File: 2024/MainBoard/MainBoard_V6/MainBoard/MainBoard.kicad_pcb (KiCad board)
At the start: 2 copper layers, 130.5 x 65 mm, 90 parts, among them J1 Raspberry_Pi_2_3, J14 UART, J15 TFT3, J16 CAN_CON, J2 fan, J3 USB_C_Receptacle_USB2.0_16P, J4 metor, J6 Debug, J8 MOLEX MINISPOX, Q1 Q_NMOS_GSD, Q2 Q_NMOS_GSD, SW1 SW_MEC_5E, SW2 Ras_1, SW3 Ras_2, SW4 SW_Wuerth_450301014042, SW5 SW_MEC_5E, SW6 SW_MEC_5E, U1 STM32F446RETx, U10 MPU9250, U11 LM1084-5.0, U2 CH340E, U3 MOUDLE-SEEEDUINO-XIAO, U6 BNO055, U7 AZ1117-3.3, U8 MAX3051, Y1 CSTNE16M0V530000R0

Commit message: 完成
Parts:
- J14: moved to B.Cu
- moved J14 6.00 mm to (43.5, 25.8), turned to 180 degrees
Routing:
- net GND: track 804.0 -> 796.6 mm, vias 69 -> 97
- net +3.3V: track 284.9 -> 290.9 mm
- net UART2_RX: track 38.8 -> 43.8 mm
- net T_CS: track 25.7 -> 26.7 mm
- net UART2_TX: track 39.0 -> 38.3 mm
- added copper zone on B.Cu, net +5V
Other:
- board text added: "16V GND"
- board text added: "5.1k"
- board text added: "D"
- board text added: "Discharge"
- board text added: "MainBoard v6"
- board text added: "← → USB SWD"
- board text removed: "MainBoard v5"
- board text removed: "USB← →SWD"

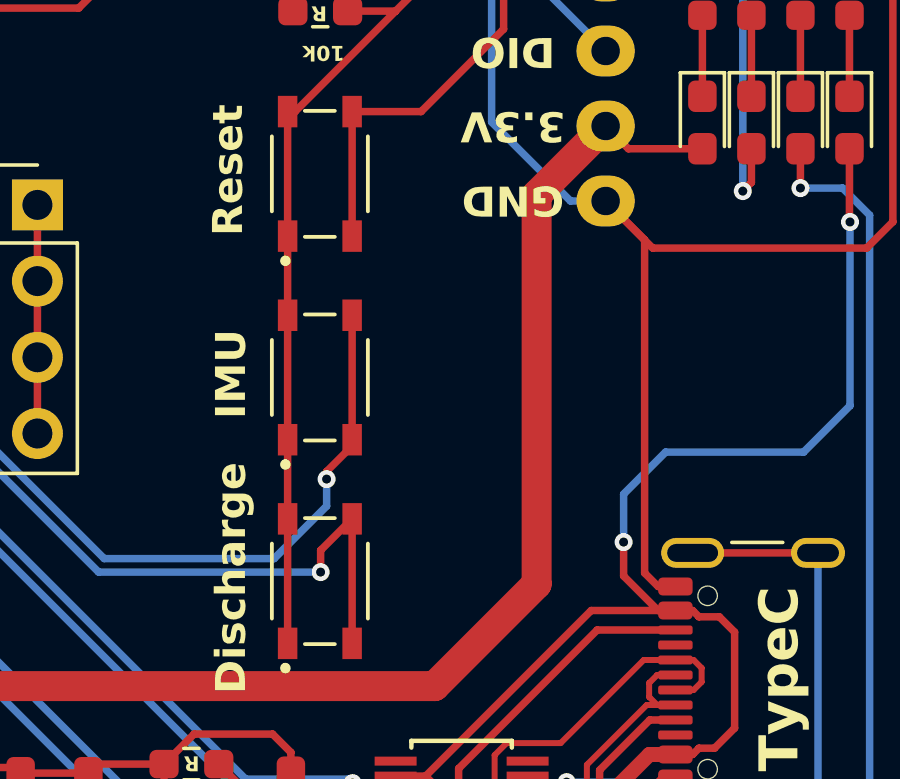
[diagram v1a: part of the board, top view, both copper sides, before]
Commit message: 差し替えver
リセットにプルアップ抵抗いれた
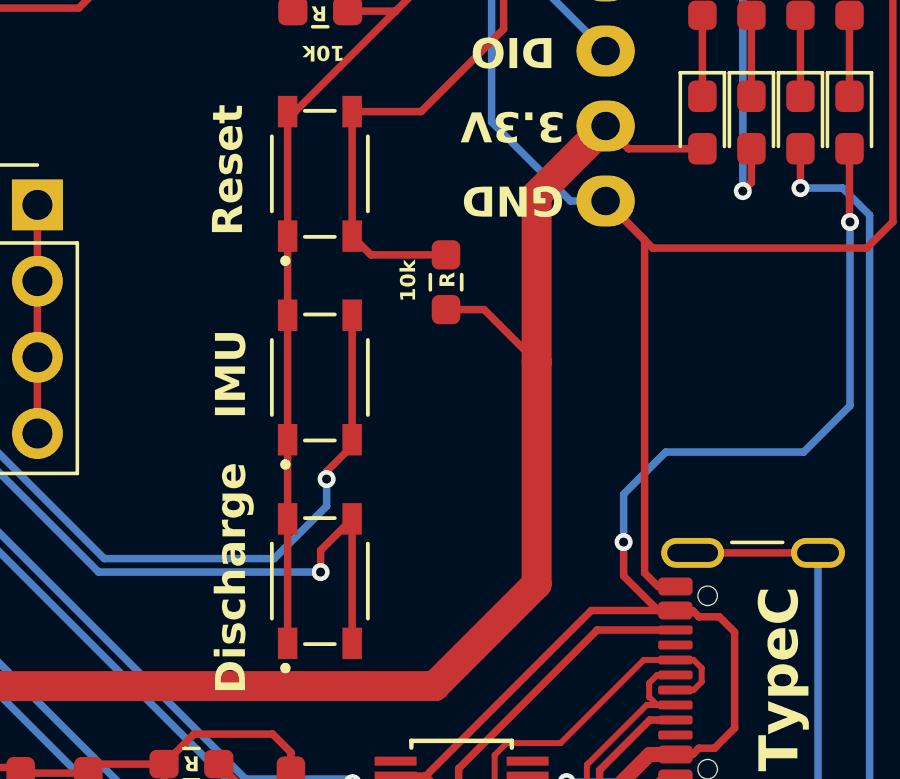
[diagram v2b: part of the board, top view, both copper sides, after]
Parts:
- added R5: 10k, Resistor_SMD:R_0603_1608Metric_Pad0.98x0.95mm_HandSolder, F.Cu at (49.2, 1.64)
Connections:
- net Kicker renamed discharge
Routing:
- net +3.3V: track 290.9 -> 294.7 mm
- net NRST: track 69.3 -> 72.7 mm
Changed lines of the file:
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@@
   (net 58 "Net-(D15-K)")
   (net 59 "SPI2.INT")
-  (net 60 "Kicker")
+  (net 60 "discharge")
   (net 61 "unconnected-(U1-PC9-Pad40)")
   (net 62 "HEART_BEAT_LED")
@@
       (net 127 "unconnected-(U1-PC6-Pad37)") (pinfunction "PC6") (pintype "bidirectional+no_connect"))
     (pad "38" smd roundrect (at 5.675 1.25) (size 1.55 0.3) (layers "F.Cu" "F.Paste" "F.Mask") (roundrect_rratio 0.25)
-      (net 60 "Kicker") (pinfunction "PC7") (pintype "bidirectional"))
+      (net 60 "discharge") (pinfunction "PC7") (pintype "bidirectional"))
     (pad "39" smd roundrect (at 5.675 0.75) (size 1.55 0.3) (layers "F.Cu" "F.Paste" "F.Mask") (roundrect_rratio 0.25)
       (net 128 "imu.reset") (pinfunction "PC8") (pintype "bidirectional"))
@@
     )
   )
+  (footprint "Resistor_SMD:R_0603_1608Metric_Pad0.98x0.95mm_HandSolder" (layer "F.Cu")
+    (at 49.18 1.6375 90)
+    (descr "Resistor SMD 0603 (1608 Metric), square (rectangular) end terminal, IPC_7351 nominal with elongated pad for handsoldering. (Body size source: IPC-SM-782 page 72, https://www.pcb-3d.com/wordpress/wp-content/uploads/ipc-sm-782a_amendment_1_and_2.pdf), generated with kicad-footprint-generator")
+    (tags "resistor handsolder")
+    (property "Sheetfile" "MainBoard.kicad_sch")
+    (property "Sheetname" "")
+    (property "ki_description" "Resistor")
+    (property "ki_keywords" "R res resistor")
+    (attr smd)
+    (fp_text reference "R5" (at 0 -1.43 90) (layer "F.SilkS") hide
+        (effects (font (size 1 1) (thickness 0.15)))
+    )
+    (fp_text value "10k" (at 0 1.43 90) (layer "F.Fab")
+        (effects (font (size 1 1) (thickness 0.15)))
+    )
+    (fp_text user "${REFERENCE}" (at 0 0 90) (layer "F.Fab")
+        (effects (font (size 0.4 0.4) (thickness 0.06)))
+    )
+    (fp_line (start -0.254724 -0.5225) (end 0.254724 -0.5225)
+      (stroke (width 0.12) (type solid)) (layer "F.SilkS"))
+    (fp_line (start -0.254724 0.5225) (end 0.254724 0.5225)
+      (stroke (width 0.12) (type solid)) (layer "F.SilkS"))
+    (fp_line (start -1.65 -0.73) (end 1.65 -0.73)
+      (stroke (width 0.05) (type solid)) (layer "F.CrtYd"))
+    (fp_line (start -1.65 0.73) (end -1.65 -0.73)
+      (stroke (width 0.05) (type solid)) (layer "F.CrtYd"))
+    (fp_line (start 1.65 -0.73) (end 1.65 0.73)
+      (stroke (width 0.05) (type solid)) (layer "F.CrtYd"))
+    (fp_line (start 1.65 0.73) (end -1.65 0.73)
+      (stroke (width 0.05) (type solid)) (layer "F.CrtYd"))
+    (fp_line (start -0.8 -0.4125) (end 0.8 -0.4125)
+      (stroke (width 0.1) (type solid)) (layer "F.Fab"))
+    (fp_line (start -0.8 0.4125) (end -0.8 -0.4125)
+      (stroke (width 0.1) (type solid)) (layer "F.Fab"))
+    (fp_line (start 0.8 -0.4125) (end 0.8 0.4125)
+      (stroke (width 0.1) (type solid)) (layer "F.Fab"))
+    (fp_line (start 0.8 0.4125) (end -0.8 0.4125)
+      (stroke (width 0.1) (type solid)) (layer "F.Fab"))
+    (pad "1" smd roundrect (at -0.9125 0 90) (size 0.975 0.95) (layers "F.Cu" "F.Paste" "F.Mask") (roundrect_rratio 0.25)
+      (net 3 "+3.3V") (pintype "passive"))
+    (pad "2" smd roundrect (at 0.9125 0 90) (size 0.975 0.95) (layers "F.Cu" "F.Paste" "F.Mask") (roundrect_rratio 0.25)
+      (net 34 "NRST") (pintype "passive"))
+    (model "${KICAD6_3DMODEL_DIR}/Resistor_SMD.3dshapes/R_0603_1608Metric.wrl"
+      (offset (xyz 0 0 0))
+      (scale (xyz 1 1 1))
+      (rotate (xyz 0 0 0))
+    )
+  )
   (footprint "LED_SMD:LED_0603_1608Metric_Pad1.05x0.95mm_HandSolder" (layer "F.Cu")
     (at 57.726 -3.686 -90)
@@
       (net 2 "GND") (pinfunction "2") (pintype "passive") (solder_mask_margin 0.102))
     (pad "3" smd rect (at -2.075 1.075 90) (size 1.05 0.65) (layers "F.Cu" "F.Paste" "F.Mask")
-      (net 60 "Kicker") (pinfunction "K") (pintype "passive") (solder_mask_margin 0.102))
+      (net 60 "discharge") (pinfunction "K") (pintype "passive") (solder_mask_margin 0.102))
     (pad "4" smd rect (at 2.075 1.075 90) (size 1.05 0.65) (layers "F.Cu" "F.Paste" "F.Mask")
-      (net 60 "Kicker") (pinfunction "A") (pintype "passive") (solder_mask_margin 0.102))
+      (net 60 "discharge") (pinfunction "A") (pintype "passive") (solder_mask_margin 0.102))
   )
   (footprint "MountingHole:MountingHole_3.2mm_M3_Pad_Via" (layer "F.Cu")
@@
     (effects (font (size 0.5 0.5) (thickness 0.1) bold) (justify bottom))
   )
+  (gr_text "10k" (at 48.21 1.59 90) (layer "F.SilkS")
+    (effects (font (size 0.5 0.5) (thickness 0.1) bold) (justify bottom))
+  )
   (gr_text "IMU" (at 42.6 4.7 90) (layer "F.SilkS")
     (effects (font (size 1 1) (thickness 0.2) bold) (justify bottom))
@@
     (effects (font (size 1 1) (thickness 0.2) bold) (justify bottom))
   )
+  (gr_text "R" (at 49.52 1.56 90) (layer "F.SilkS")
+    (effects (font (size 0.5 0.5) (thickness 0.1) bold) (justify bottom))
+  )
   (gr_text "CLK" (at 51.41 -9.1 180) (layer "F.SilkS")
     (effects (font (size 1 1) (thickness 0.2) bold) (justify bottom))
@@
   (segment (start 19.46 24.09) (end 26.81 24.09) (width 0.5) (layer "F.Cu") (net 3))
   (segment (start 21.029 5.08) (end 20.745 4.796) (width 0.25) (layer "F.Cu") (net 3))
+  (segment (start 50.45 2.55) (end 52.2 4.3) (width 0.25) (layer "F.Cu") (net 3))
   (segment (start 17.833 -10.414) (end 14.986 -10.414) (width 1) (layer "F.Cu") (net 3))
   (segment (start 5.969 2.289) (end 5.969 3.937) (width 0.25) (layer "F.Cu") (net 3))
@@
   (segment (start 28.2 22.7) (end 29.5 24) (width 0.5) (layer "F.Cu") (net 3))
   (segment (start 6.096 4.064) (end 2.5654 4.064) (width 1) (layer "F.Cu") (net 3))
+  (segment (start 52.2 4.3) (end 52.2 -1.27) (width 1) (layer "F.Cu") (net 3))
   (segment (start 27.8515 7.5) (end 30.1405 5.211) (width 1) (layer "F.Cu") (net 3))
   (segment (start 11.5 0.25) (end 11.5 -3.88) (width 1) (layer "F.Cu") (net 3))
@@
   (segment (start 13.95915 2.0817) (end 13.75 2.0817) (width 0.25) (layer "F.Cu") (net 3))
   (segment (start 57.726 -2.811) (end 55.259 -2.811) (width 0.25) (layer "F.Cu") (net 3))
-  (segment (start 52.2 11.7) (end 52.2 -1.27) (width 1) (layer "F.Cu") (net 3))
   (segment (start 15.0865 7.239) (end 15.0865 8.83) (width 1) (layer "F.Cu") (net 3))
   (segment (start 17.833 -10.414) (end 19.745 -8.502) (width 0.25) (layer "F.Cu") (net 3))
@@
   (segment (start 28.2 20.015184) (end 29.8 18.415184) (width 0.5) (layer "F.Cu") (net 3))
   (segment (start 14.75 1.29085) (end 13.95915 2.0817) (width 0.25) (layer "F.Cu") (net 3))
+  (segment (start 52.2 11.7) (end 52.2 4.3) (width 1) (layer "F.Cu") (net 3))
   (segment (start 31.7515 -7.5) (end 36.936396 -7.5) (width 0.25) (layer "F.Cu") (net 3))
   (segment (start -2.4892 -3.7084) (end -2.6924 -3.7084) (width 1) (layer "F.Cu") (net 3))
@@
   (segment (start -2.8194 -3.8354) (end -2.8194 -8.9154) (width 1) (layer "F.Cu") (net 3))
   (segment (start 15.0865 8.83) (end 18.228 8.83) (width 1) (layer "F.Cu") (net 3))
+  (segment (start 49.18 2.55) (end 50.45 2.55) (width 0.25) (layer "F.Cu") (net 3))
   (segment (start -49.1 19.2) (end -49.1 -12.2) (width 1) (layer "F.Cu") (net 3))
   (segment (start 0.1016 1.6002) (end 0.1016 -1.1176) (width 1) (layer "F.Cu") (net 3))
@@
   (segment (start 51.1 -6.8) (end 48.35 -4.05) (width 0.25) (layer "F.Cu") (net 34))
   (segment (start 51.1 -9.6) (end 52.57 -11.07) (width 0.25) (layer "F.Cu") (net 34))
+  (segment (start 49.18 0.725) (end 46.675 0.725) (width 0.25) (layer "F.Cu") (net 34))
   (segment (start 52.57 -11.07) (end 54.5 -11.07) (width 0.25) (layer "F.Cu") (net 34))
   (segment (start 19.208059 -3.669) (end 19.083059 -3.544) (width 0.25) (layer "F.Cu") (net 34))
@@
   (segment (start 51.1 -9.6) (end 51.1 -6.8) (width 0.25) (layer "F.Cu") (net 34))
   (segment (start 46.05 -4.05) (end 48.35 -4.05) (width 0.25) (layer "F.Cu") (net 34))
+  (segment (start 46.675 0.725) (end 46.05 0.1) (width 0.25) (layer "F.Cu") (net 34))
   (via (at 19.208059 -3.669) (size 0.6) (drill 0.3) (layers "F.Cu" "B.Cu") (net 34))
   (segment (start 36.9 -19.5) (end 50.2 -19.5) (width 0.25) (layer "B.Cu") (net 34))
